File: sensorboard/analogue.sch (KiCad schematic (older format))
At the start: 15 parts

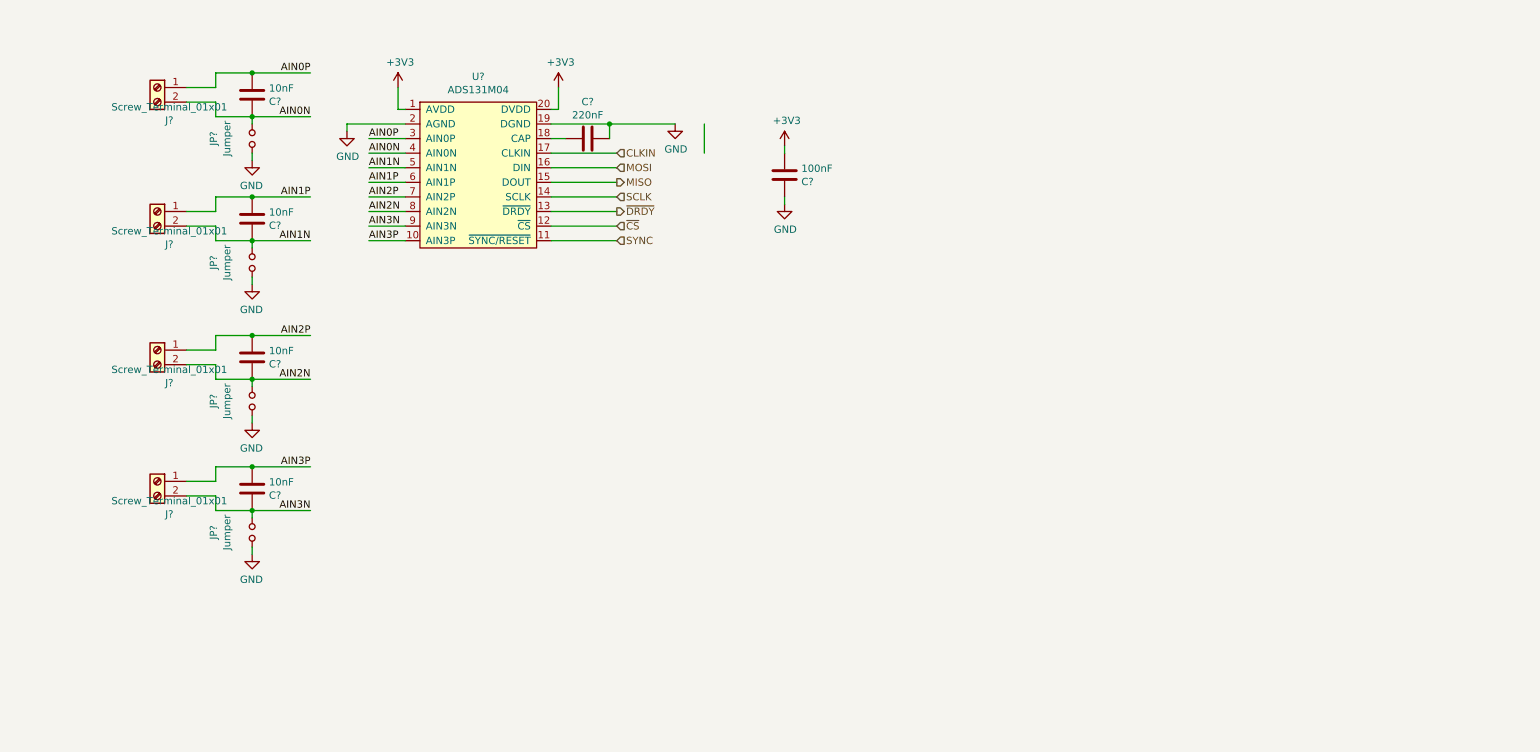
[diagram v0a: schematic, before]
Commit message: Voltage divider setup
Voltage divider setup, removed unused components, CAN RX/TX empty for now (waiting for kiran)
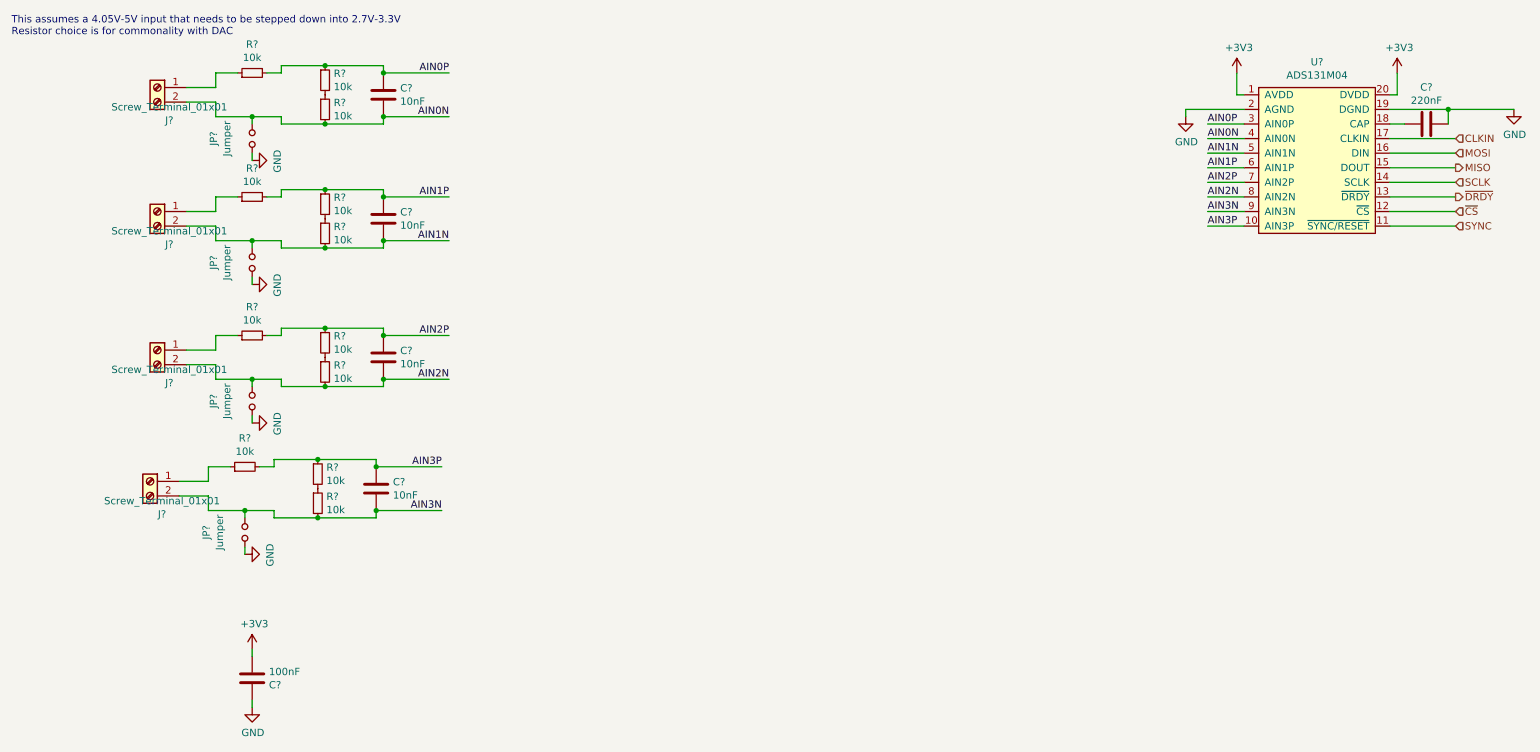
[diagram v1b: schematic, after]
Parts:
- removed C? (x3): 10nF, Capacitor_SMD:C_0603_1608Metric, symbol Device:C
- removed J? (x3): Screw_Terminal_01x01, TerminalBlock_Phoenix:TerminalBlock_Phoenix_MPT-2.54mm_2pol, symbol Connector:Screw_Terminal_01x02
- removed JP? (x3): Jumper, Connector_PinHeader_2.54mm:PinHeader_1x02_P2.54mm_Vertical, symbol Device:Jumper_NO_Small
- added C? (x3): 10nF, Capacitor_SMD:C_0603_1608Metric, symbol Device:C
- added J? (x3): Screw_Terminal_01x01, TerminalBlock_Phoenix:TerminalBlock_Phoenix_MPT-2.54mm_2pol, symbol Connector:Screw_Terminal_01x02
- added JP? (x3): Jumper, Connector_PinHeader_2.54mm:PinHeader_1x02_P2.54mm_Vertical, symbol Device:Jumper_NO_Small
- added R? (x12): 10k, symbol Device:R_Small
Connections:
- net AIN0N: now also C?.2, R?.2; no longer C?.1
- net AIN0P: now also C?.1, R?.1, R?.2; no longer C?.2, J?.1 (Pin_1)
- net AIN1N: now also C?.2, J?.2 (Pin_2), JP?.1, R?.2
- net AIN1P: now also C?.1, R?.1, R?.2
- net AIN2N: now also C?.2, J?.2 (Pin_2), JP?.1, R?.2
- net AIN2P: now also C?.1, R?.1, R?.2
- net AIN3N: now also C?.2, J?.2 (Pin_2), JP?.1, R?.2
- net AIN3P: now also C?.1, R?.1, R?.2
- net GND: now also JP?.2, JP?.2, JP?.2
- new net: J?.1 (Pin_1), R?.1 (x4)
- new net: R?.1, R?.2 (x4)
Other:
- note added: "This assumes a 4.05V-5V input that needs to be stepped down into 2.7V-3.3V\nResistor choice is for commonality with DAC"
- moved on the sheet: C?, U?

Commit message: Minor edits
descriptors
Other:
- note added: "This assumes a 0V-5V input that needs to be scaled down into 0V-3.3V\nResistor choice is for commonality with DAC"
- note removed: "This assumes a 4.05V-5V input that needs to be stepped down into 2.7V-3.3V\nResistor choice is for commonality with DAC"
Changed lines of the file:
@@
 $Descr A4 11693 8268
 encoding utf-8
-Sheet 3 5
+Sheet 5 5
 Title ""
 Date ""
@@
 Connection ~ 2700 850
 Text Notes 550  650  0    50   ~ 0
-This assumes a 4.05V-5V input that needs to be stepped down into 2.7V-3.3V\nResistor choice is for commonality with DAC
+This assumes a 0V-5V input that needs to be scaled down into 0V-3.3V\nResistor choice is for commonality with DAC
 $Comp
 L Device:C C?

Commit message: I2C ADC conversion+MCP31856 x10
As above xD
just need to do the pcb layout
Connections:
- net AIN0N: no longer C?.2, J?.2 (Pin_2), JP?.1, R?.2
- net GND: now also C?.2, J?.2 (Pin_2), JP?.1, R?.2
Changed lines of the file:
@@
 $Descr A4 11693 8268
 encoding utf-8
-Sheet 5 5
+Sheet 4 4
 Title ""
 Date ""
@@
 AR Path="/61CE5E8C/5DB4AADD" Ref="#PWR?"  Part="1"
 AR Path="/61D24785/5DB4AADD" Ref="#PWR?"  Part="1"
+AR Path="/61BCFD2E/5DB4AADD" Ref="#PWR?"  Part="1"
 F 0 "#PWR?" H 10850 900 50  0001 C CNN
 F 1 "GND" H 10855 977 50  0000 C CNN
@@
 AR Path="/61CE5E8C/5DB760F5" Ref="#PWR?"  Part="1"
 AR Path="/61D24785/5DB760F5" Ref="#PWR?"  Part="1"
+AR Path="/61BCFD2E/5DB760F5" Ref="#PWR?"  Part="1"
 F 0 "#PWR?" H 8600 950 50  0001 C CNN
 F 1 "GND" H 8605 1027 50  0000 C CNN
@@
 AR Path="/61CE5E8C/5DB818AE" Ref="C?"  Part="1"
 AR Path="/61D24785/5DB818AE" Ref="C?"  Part="1"
+AR Path="/61BCFD2E/5DB818AE" Ref="C?"  Part="1"
 F 0 "C?" V 9998 1250 50  0000 C CNN
 F 1 "220nF" V 10089 1250 50  0000 C CNN
@@
 AR Path="/61CE5E8C/5DB84339" Ref="#PWR?"  Part="1"
 AR Path="/61D24785/5DB84339" Ref="#PWR?"  Part="1"
+AR Path="/61BCFD2E/5DB84339" Ref="#PWR?"  Part="1"
 F 0 "#PWR?" H 10050 750 50  0001 C CNN
 F 1 "+3V3" H 10065 1073 50  0000 C CNN
@@
 AR Path="/61CE5E8C/5DB85107" Ref="#PWR?"  Part="1"
 AR Path="/61D24785/5DB85107" Ref="#PWR?"  Part="1"
+AR Path="/61BCFD2E/5DB85107" Ref="#PWR?"  Part="1"
 F 0 "#PWR?" H 8950 750 50  0001 C CNN
 F 1 "+3V3" H 8965 1073 50  0000 C CNN
@@
 Text Label 8750 1950 0    50   ~ 0
 AIN3P
-Text Label 3550 1200 2    50   ~ 0
-AIN0N
 Text Label 3550 2050 2    50   ~ 0
 AIN1N
@@
 AR Path="/61CE5E8C/5DC4E710" Ref="JP?"  Part="1"
 AR Path="/61D24785/5DC4E710" Ref="JP?"  Part="1"
+AR Path="/61BCFD2E/5DC4E710" Ref="JP?"  Part="1"
 F 0 "JP?" H 2200 1614 50  0000 C CNN
 F 1 "Jumper" H 2200 1523 50  0000 C CNN
@@
 AR Path="/61CE5E8C/5DC4E71A" Ref="J?"  Part="1"
 AR Path="/61D24785/5DC4E71A" Ref="J?"  Part="1"
+AR Path="/61BCFD2E/5DC4E71A" Ref="J?"  Part="1"
 F 0 "J?" H 1468 775 50  0000 C CNN
 F 1 "Screw_Terminal_01x01" H 1468 866 50  0000 C CNN
@@
 AR Path="/61CE5E8C/5DC4E725" Ref="#PWR?"  Part="1"
 AR Path="/61D24785/5DC4E725" Ref="#PWR?"  Part="1"
+AR Path="/61BCFD2E/5DC4E725" Ref="#PWR?"  Part="1"
 F 0 "#PWR?" H 2200 1250 50  0001 C CNN
 F 1 "GND" H 2205 1327 50  0000 C CNN
@@
 AR Path="/61CE5E8C/61B95E91" Ref="U?"  Part="1"
 AR Path="/61D24785/61B95E91" Ref="U?"  Part="1"
+AR Path="/61BCFD2E/61B95E91" Ref="U?"  Part="1"
 F 0 "U?" H 9500 2175 50  0000 C CNN
 F 1 "ADS131M04" H 9500 2084 50  0000 C CNN
@@
 AR Path="/61CE5E8C/5E1BB739" Ref="#PWR?"  Part="1"
 AR Path="/61D24785/5E1BB739" Ref="#PWR?"  Part="1"
+AR Path="/61BCFD2E/5E1BB739" Ref="#PWR?"  Part="1"
 F 0 "#PWR?" H 2200 5000 50  0001 C CNN
 F 1 "GND" H 2205 5077 50  0000 C CNN
@@
 AR Path="/61CE5E8C/5E1BB1FA" Ref="#PWR?"  Part="1"
 AR Path="/61D24785/5E1BB1FA" Ref="#PWR?"  Part="1"
+AR Path="/61BCFD2E/5E1BB1FA" Ref="#PWR?"  Part="1"
 F 0 "#PWR?" H 2200 4700 50  0001 C CNN
 F 1 "+3V3" H 2215 5023 50  0000 C CNN
@@
 AR Path="/61CE5E8C/5E1BAB7F" Ref="C?"  Part="1"
 AR Path="/61D24785/5E1BAB7F" Ref="C?"  Part="1"
+AR Path="/61BCFD2E/5E1BAB7F" Ref="C?"  Part="1"
 F 0 "C?" H 2315 5096 50  0000 L CNN
 F 1 "100nF" H 2315 5005 50  0000 L CNN
@@
 AR Path="/61B8DF6C/6193849D" Ref="R?"  Part="1"
 AR Path="/61D24785/6193849D" Ref="R?"  Part="1"
+AR Path="/61BCFD2E/6193849D" Ref="R?"  Part="1"
 F 0 "R?" V 2396 900 50  0000 C CNN
 F 1 "10k" V 2305 900 50  0000 C CNN
@@
 AR Path="/61B8DF6C/61955A05" Ref="R?"  Part="1"
 AR Path="/61D24785/61955A05" Ref="R?"  Part="1"
+AR Path="/61BCFD2E/61955A05" Ref="R?"  Part="1"
 F 0 "R?" H 2759 996 50  0000 L CNN
 F 1 "10k" H 2759 905 50  0000 L CNN
@@
 AR Path="/61B8DF6C/61955DE5" Ref="R?"  Part="1"
 AR Path="/61D24785/61955DE5" Ref="R?"  Part="1"
+AR Path="/61BCFD2E/61955DE5" Ref="R?"  Part="1"
 F 0 "R?" H 2759 1196 50  0000 L CNN
 F 1 "10k" H 2759 1105 50  0000 L CNN
@@
 AR Path="/61CE5E8C/5DC4E705" Ref="C?"  Part="1"
 AR Path="/61D24785/5DC4E705" Ref="C?"  Part="1"
+AR Path="/61BCFD2E/5DC4E705" Ref="C?"  Part="1"
 F 0 "C?" H 3215 1096 50  0000 L CNN
 F 1 "10nF" H 3215 1005 50  0000 L CNN
@@
 AR Path="/61CE5E8C/6199C4C3" Ref="JP?"  Part="1"
 AR Path="/61D24785/6199C4C3" Ref="JP?"  Part="1"
+AR Path="/61BCFD2E/6199C4C3" Ref="JP?"  Part="1"
 F 0 "JP?" H 2200 2464 50  0000 C CNN
 F 1 "Jumper" H 2200 2373 50  0000 C CNN
@@
 AR Path="/61CE5E8C/6199C4C9" Ref="J?"  Part="1"
 AR Path="/61D24785/6199C4C9" Ref="J?"  Part="1"
+AR Path="/61BCFD2E/6199C4C9" Ref="J?"  Part="1"
 F 0 "J?" H 1468 1625 50  0000 C CNN
 F 1 "Screw_Terminal_01x01" H 1468 1716 50  0000 C CNN
@@
 AR Path="/61CE5E8C/6199C4D0" Ref="#PWR?"  Part="1"
 AR Path="/61D24785/6199C4D0" Ref="#PWR?"  Part="1"
+AR Path="/61BCFD2E/6199C4D0" Ref="#PWR?"  Part="1"
 F 0 "#PWR?" H 2200 2100 50  0001 C CNN
 F 1 "GND" H 2205 2177 50  0000 C CNN
@@
 AR Path="/61B8DF6C/6199C4DC" Ref="R?"  Part="1"
 AR Path="/61D24785/6199C4DC" Ref="R?"  Part="1"
+AR Path="/61BCFD2E/6199C4DC" Ref="R?"  Part="1"
 F 0 "R?" V 2396 1750 50  0000 C CNN
 F 1 "10k" V 2305 1750 50  0000 C CNN
@@
 AR Path="/61B8DF6C/6199C4E3" Ref="R?"  Part="1"
 AR Path="/61D24785/6199C4E3" Ref="R?"  Part="1"
+AR Path="/61BCFD2E/6199C4E3" Ref="R?"  Part="1"
 F 0 "R?" H 2759 1846 50  0000 L CNN
 F 1 "10k" H 2759 1755 50  0000 L CNN
@@
 AR Path="/61B8DF6C/6199C4E9" Ref="R?"  Part="1"
 AR Path="/61D24785/6199C4E9" Ref="R?"  Part="1"
+AR Path="/61BCFD2E/6199C4E9" Ref="R?"  Part="1"
 F 0 "R?" H 2759 2046 50  0000 L CNN
 F 1 "10k" H 2759 1955 50  0000 L CNN
@@
 AR Path="/61CE5E8C/6199C4FA" Ref="C?"  Part="1"
 AR Path="/61D24785/6199C4FA" Ref="C?"  Part="1"
+AR Path="/61BCFD2E/6199C4FA" Ref="C?"  Part="1"
 F 0 "C?" H 3215 1946 50  0000 L CNN
 F 1 "10nF" H 3215 1855 50  0000 L CNN
@@
 AR Path="/61CE5E8C/619A1BB3" Ref="JP?"  Part="1"
 AR Path="/61D24785/619A1BB3" Ref="JP?"  Part="1"
+AR Path="/61BCFD2E/619A1BB3" Ref="JP?"  Part="1"
 F 0 "JP?" H 2200 3414 50  0000 C CNN
 F 1 "Jumper" H 2200 3323 50  0000 C CNN
@@
 AR Path="/61CE5E8C/619A1BB9" Ref="J?"  Part="1"
 AR Path="/61D24785/619A1BB9" Ref="J?"  Part="1"
+AR Path="/61BCFD2E/619A1BB9" Ref="J?"  Part="1"
 F 0 "J?" H 1468 2575 50  0000 C CNN
 F 1 "Screw_Terminal_01x01" H 1468 2666 50  0000 C CNN
@@
 AR Path="/61CE5E8C/619A1BC0" Ref="#PWR?"  Part="1"
 AR Path="/61D24785/619A1BC0" Ref="#PWR?"  Part="1"
+AR Path="/61BCFD2E/619A1BC0" Ref="#PWR?"  Part="1"
 F 0 "#PWR?" H 2200 3050 50  0001 C CNN
 F 1 "GND" H 2205 3127 50  0000 C CNN
@@
 AR Path="/61B8DF6C/619A1BCC" Ref="R?"  Part="1"
 AR Path="/61D24785/619A1BCC" Ref="R?"  Part="1"
+AR Path="/61BCFD2E/619A1BCC" Ref="R?"  Part="1"
 F 0 "R?" V 2396 2700 50  0000 C CNN
 F 1 "10k" V 2305 2700 50  0000 C CNN
@@
 AR Path="/61B8DF6C/619A1BD3" Ref="R?"  Part="1"
 AR Path="/61D24785/619A1BD3" Ref="R?"  Part="1"
+AR Path="/61BCFD2E/619A1BD3" Ref="R?"  Part="1"
 F 0 "R?" H 2759 2796 50  0000 L CNN
 F 1 "10k" H 2759 2705 50  0000 L CNN
@@
 AR Path="/61B8DF6C/619A1BD9" Ref="R?"  Part="1"
 AR Path="/61D24785/619A1BD9" Ref="R?"  Part="1"
+AR Path="/61BCFD2E/619A1BD9" Ref="R?"  Part="1"
 F 0 "R?" H 2759 2996 50  0000 L CNN
 F 1 "10k" H 2759 2905 50  0000 L CNN
@@
 AR Path="/61CE5E8C/619A1BEA" Ref="C?"  Part="1"
 AR Path="/61D24785/619A1BEA" Ref="C?"  Part="1"
+AR Path="/61BCFD2E/619A1BEA" Ref="C?"  Part="1"
 F 0 "C?" H 3215 2896 50  0000 L CNN
 F 1 "10nF" H 3215 2805 50  0000 L CNN
@@
 AR Path="/61CE5E8C/619B0B1C" Ref="JP?"  Part="1"
 AR Path="/61D24785/619B0B1C" Ref="JP?"  Part="1"
+AR Path="/61BCFD2E/619B0B1C" Ref="JP?"  Part="1"
 F 0 "JP?" H 2150 4314 50  0000 C CNN
 F 1 "Jumper" H 2150 4223 50  0000 C CNN
@@
 AR Path="/61CE5E8C/619B0B22" Ref="J?"  Part="1"
 AR Path="/61D24785/619B0B22" Ref="J?"  Part="1"
+AR Path="/61BCFD2E/619B0B22" Ref="J?"  Part="1"
 F 0 "J?" H 1418 3475 50  0000 C CNN
 F 1 "Screw_Terminal_01x01" H 1418 3566 50  0000 C CNN
@@
 AR Path="/61CE5E8C/619B0B29" Ref="#PWR?"  Part="1"
 AR Path="/61D24785/619B0B29" Ref="#PWR?"  Part="1"
+AR Path="/61BCFD2E/619B0B29" Ref="#PWR?"  Part="1"
 F 0 "#PWR?" H 2150 3950 50  0001 C CNN
 F 1 "GND" H 2155 4027 50  0000 C CNN
@@
 AR Path="/61B8DF6C/619B0B35" Ref="R?"  Part="1"
 AR Path="/61D24785/619B0B35" Ref="R?"  Part="1"
+AR Path="/61BCFD2E/619B0B35" Ref="R?"  Part="1"
 F 0 "R?" V 2346 3600 50  0000 C CNN
 F 1 "10k" V 2255 3600 50  0000 C CNN
@@
 AR Path="/61B8DF6C/619B0B3C" Ref="R?"  Part="1"
 AR Path="/61D24785/619B0B3C" Ref="R?"  Part="1"
+AR Path="/61BCFD2E/619B0B3C" Ref="R?"  Part="1"
 F 0 "R?" H 2709 3696 50  0000 L CNN
 F 1 "10k" H 2709 3605 50  0000 L CNN
@@
 AR Path="/61B8DF6C/619B0B42" Ref="R?"  Part="1"
 AR Path="/61D24785/619B0B42" Ref="R?"  Part="1"
+AR Path="/61BCFD2E/619B0B42" Ref="R?"  Part="1"
 F 0 "R?" H 2709 3896 50  0000 L CNN
 F 1 "10k" H 2709 3805 50  0000 L CNN
@@
 AR Path="/61CE5E8C/619B0B53" Ref="C?"  Part="1"
 AR Path="/61D24785/619B0B53" Ref="C?"  Part="1"
+AR Path="/61BCFD2E/619B0B53" Ref="C?"  Part="1"
 F 0 "C?" H 3165 3796 50  0000 L CNN
 F 1 "10nF" H 3165 3705 50  0000 L CNN
@@
 Wire Wire Line
 	3050 3600 3500 3600
+$Comp
+L power:GND #PWR?
+U 1 1 61BDFEB1
+P 3550 1200
+F 0 "#PWR?" H 3550 950 50  0001 C CNN
+F 1 "GND" V 3555 1072 50  0000 R CNN
+F 2 "" H 3550 1200 50  0001 C CNN
+F 3 "" H 3550 1200 50  0001 C CNN
+	1    3550 1200
+	0    -1   -1   0
+$EndComp
 $EndSCHEMATC
